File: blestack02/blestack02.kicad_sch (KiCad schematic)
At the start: 21 parts, among them J1 UART, J2 VIN, SW1 RST, SW2 BOOT, U1 AMS1117-3.3, U2 ESP32-WROOM-32

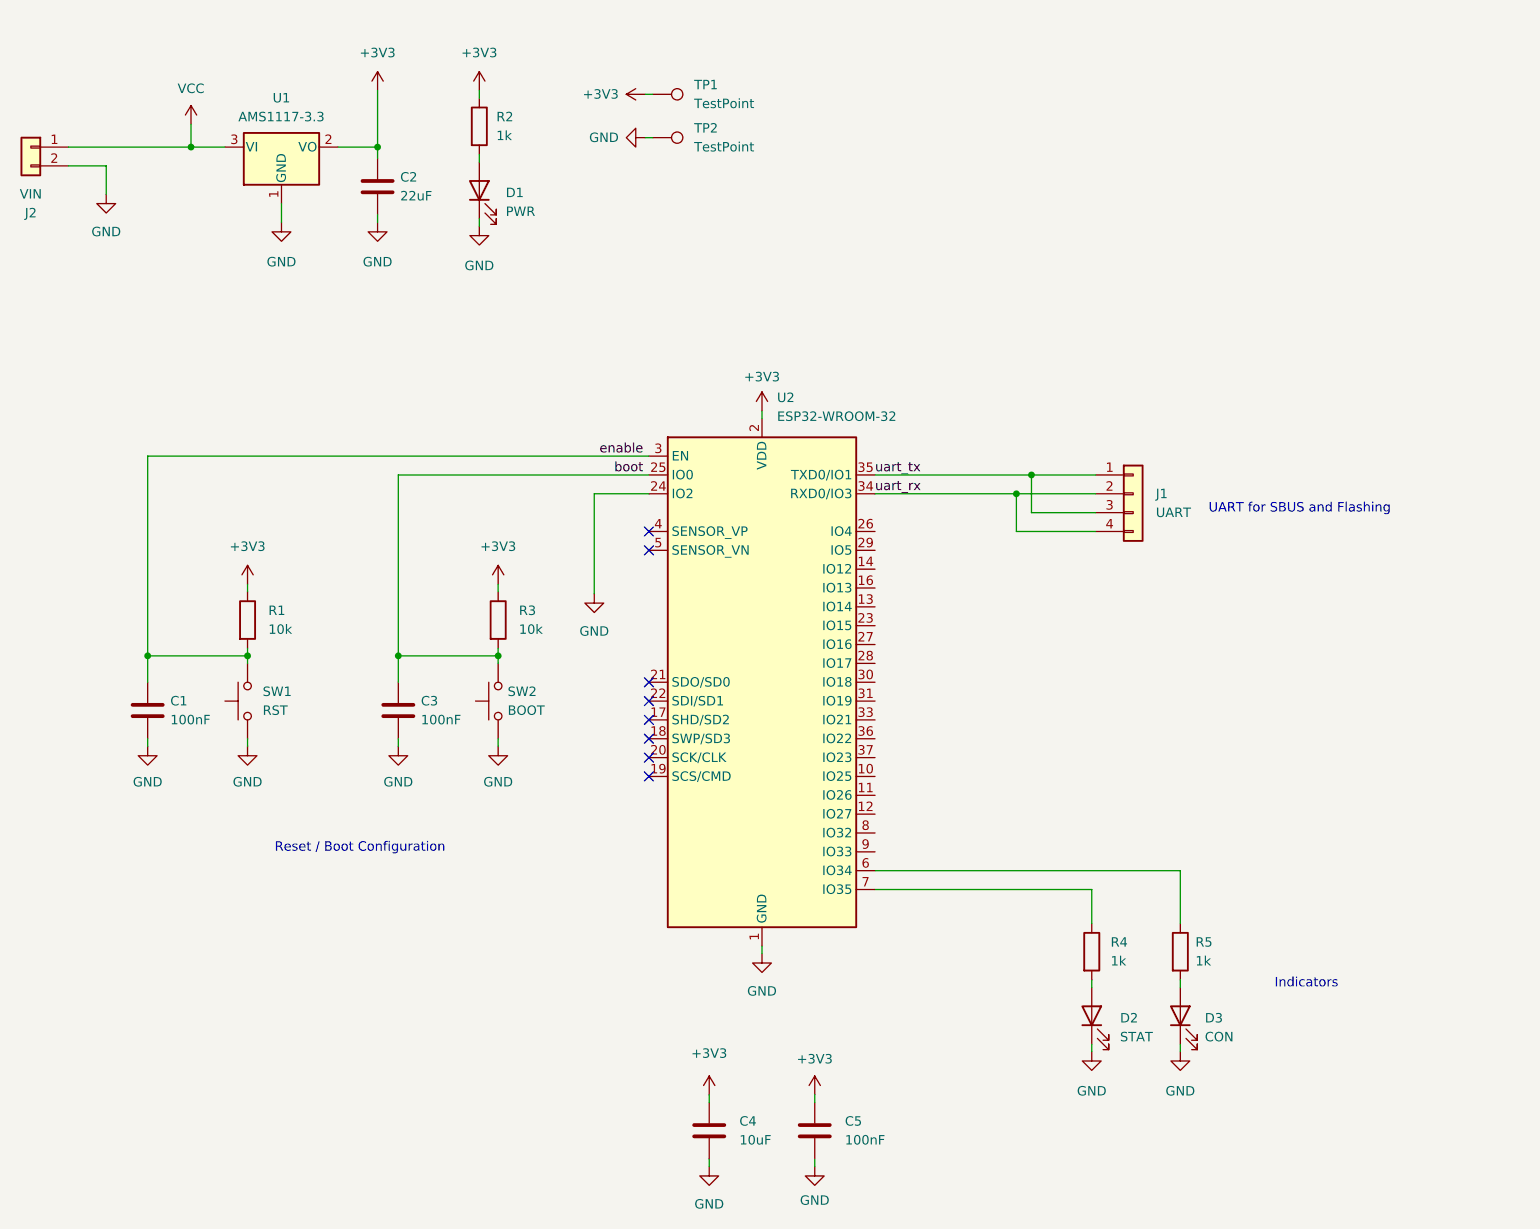
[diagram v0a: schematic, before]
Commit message: [blestack02] Update pins for stat and con leds
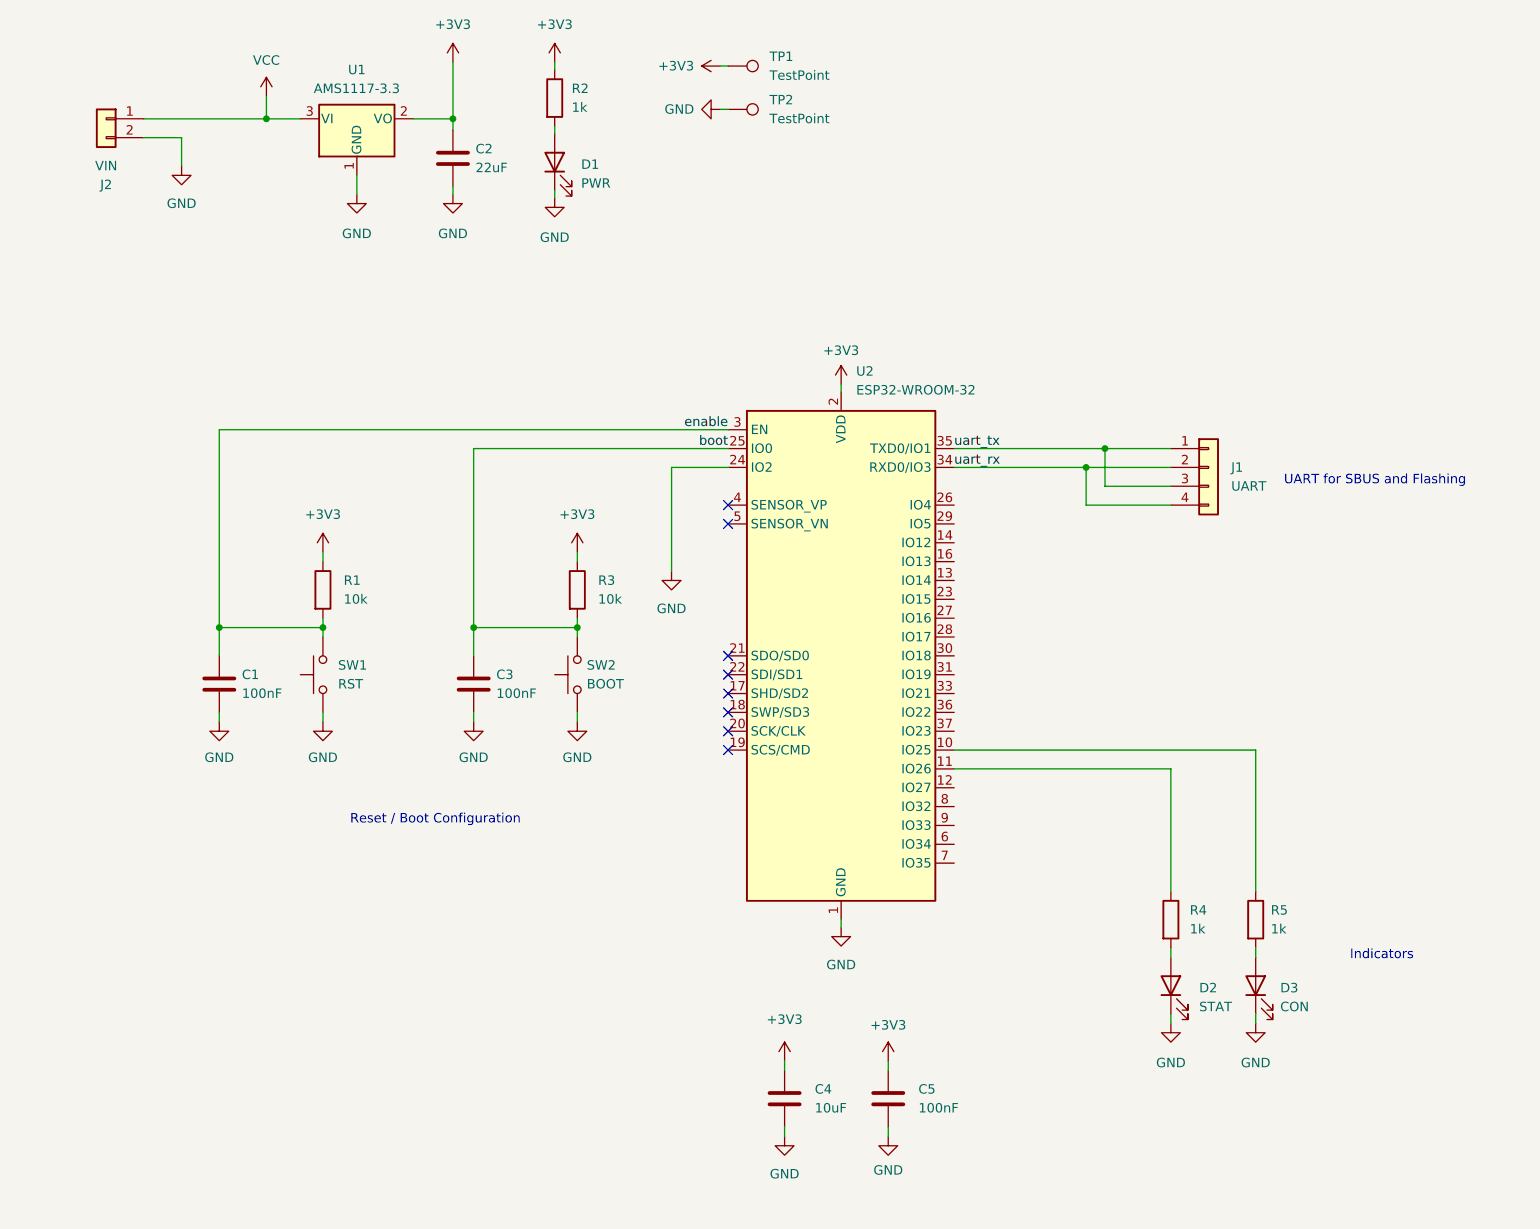
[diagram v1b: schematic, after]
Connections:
- net at R5.1: now also U2.10 (IO25); no longer U2.6 (IO34)
- net at R4.1: now also U2.11 (IO26); no longer U2.7 (IO35)
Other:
- moved on the sheet: C1, C2, C3, C4, C5, D1, D2, D3, J1, J2, R1, R2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

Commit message: update LED JLCPCB part number
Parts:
- D2: LCSC C72043 -> C5252984
- D3: LCSC C72041 -> C5197644
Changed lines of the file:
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@@
 			)
 		)
-		(property "Datasheet" "~"
+		(property "Datasheet" "https://wmsc.lcsc.com/wmsc/upload/file/pdf/v2/lcsc/2306061155_Wurth-Elektronik-150060GS75000_C5252984.pdf"
 			(at 186.69 147.32 0)
 			(effects
@@
 			)
 		)
-		(property "LCSC" "C72043"
+		(property "LCSC" "C5252984"
 			(at 186.69 147.32 90)
 			(effects
@@
 			)
 		)
-		(property "Datasheet" ""
+		(property "Datasheet" "https://wmsc.lcsc.com/wmsc/upload/file/pdf/v2/lcsc/2306061153_Wurth-Elektronik-150060BS75000_C5197644.pdf"
 			(at 198.12 147.32 0)
 			(effects
@@
 			)
 		)
-		(property "LCSC" "C72041"
+		(property "LCSC" "C5197644"
 			(at 198.12 147.32 90)
 			(effects
